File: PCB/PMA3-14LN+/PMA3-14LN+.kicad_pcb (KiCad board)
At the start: 4 copper layers, 35 x 35 mm, 26 parts, among them U1 PMA3-14LN+, U2 L7806

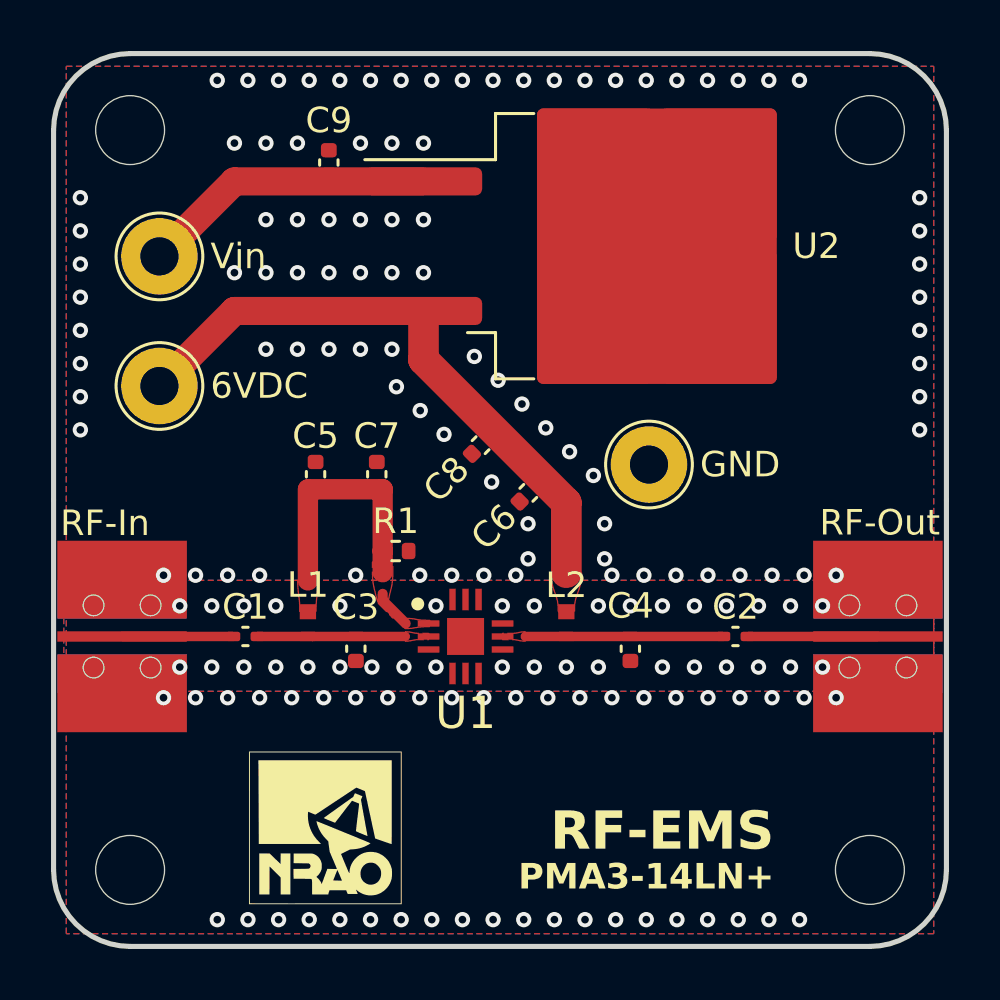
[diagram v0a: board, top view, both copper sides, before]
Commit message: pcb: added boms, updated readmes, changed silkscreen from dfs/ems to nmsm
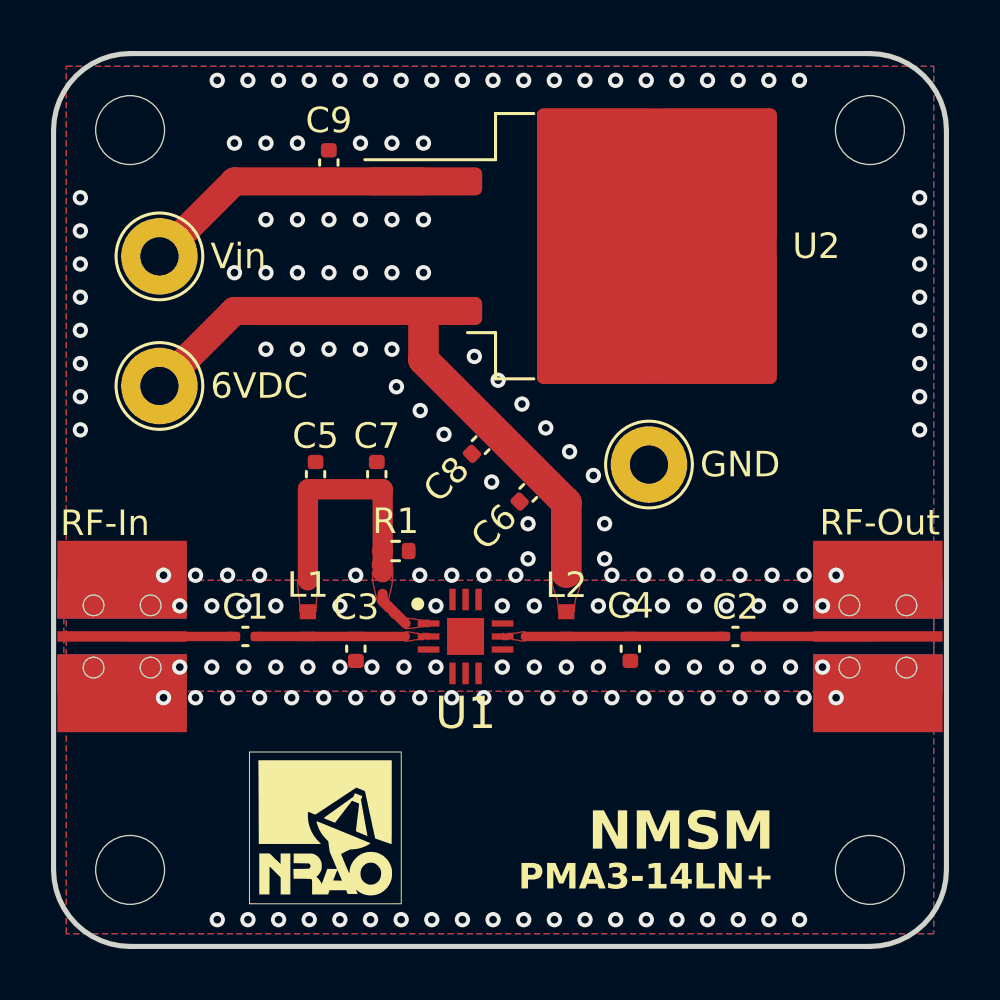
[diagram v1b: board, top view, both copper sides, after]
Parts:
- renumbered RF-In to J1, RF-Out to J2, GND to TP1, Vin to TP2, 6VDC to TP3
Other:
- board text added: "NMSM"
- board text removed: "RF-EMS"
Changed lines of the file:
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@@
     (property "ki_keywords" "test point tp")
     (attr through_hole)
-    (fp_text reference "GND" (at 2 0) (layer "F.SilkS")
+    (fp_text reference "TP1" (at 2 0) (layer "F.Fab")
         (effects (font (size 1 1) (thickness 0.15)) (justify left))
     )
@@
         (effects (font (size 1 1) (thickness 0.15)))
     )
-    (fp_text user "${REFERENCE}" (at 0.7 2.5) (layer "F.Fab")
-        (effects (font (size 1 1) (thickness 0.15)))
+    (fp_text user "GND" (at 2 0) (layer "F.SilkS")
+        (effects (font (size 1 1) (thickness 0.15)) (justify left))
     )
     (fp_circle (center 0 0) (end 1.7 0)
@@
     (property "ki_keywords" "BNC SMA SMB SMC LEMO coaxial connector CINCH RCA")
     (attr smd)
-    (fp_text reference "RF-Out" (at -4.29 4.46 180) (layer "F.SilkS")
+    (fp_text reference "J2" (at -4.29 4.46 180) (layer "F.Fab")
         (effects (font (size 1 1) (thickness 0.15)) (justify right))
     )
@@
         (effects (font (size 1 1) (thickness 0.15)))
     )
-    (fp_text user "${REFERENCE}" (at -1.5 7 180) (layer "F.Fab")
-        (effects (font (size 1 1) (thickness 0.15)))
+    (fp_text user "RF-Out" (at -4.29 4.46 180) (layer "F.SilkS")
+        (effects (font (size 1 1) (thickness 0.15)) (justify right))
     )
     (fp_circle (center -2.9718 -1.2192) (end -2.5654 -1.2192)
@@
     (property "ki_keywords" "test point tp")
     (attr through_hole)
-    (fp_text reference "6VDC" (at 2 0) (layer "F.SilkS")
+    (fp_text reference "TP3" (at 2 0) (layer "F.Fab")
         (effects (font (size 1 1) (thickness 0.15)) (justify left))
     )
@@
         (effects (font (size 1 1) (thickness 0.15)))
     )
-    (fp_text user "${REFERENCE}" (at 0.7 2.5) (layer "F.Fab")
-        (effects (font (size 1 1) (thickness 0.15)))
+    (fp_text user "6VDC" (at 2 0) (layer "F.SilkS")
+        (effects (font (size 1 1) (thickness 0.15)) (justify left))
     )
     (fp_circle (center 0 0) (end 1.7 0)
@@
     (property "ki_keywords" "test point tp")
     (attr through_hole)
-    (fp_text reference "Vin" (at 2 0) (layer "F.SilkS")
+    (fp_text reference "TP2" (at 2 0) (layer "F.Fab")
         (effects (font (size 1 1) (thickness 0.15)) (justify left))
     )
@@
         (effects (font (size 1 1) (thickness 0.15)))
     )
-    (fp_text user "${REFERENCE}" (at 0.7 2.5) (layer "F.Fab")
-        (effects (font (size 1 1) (thickness 0.15)))
+    (fp_text user "Vin" (at 2 0) (layer "F.SilkS")
+        (effects (font (size 1 1) (thickness 0.15)) (justify left))
     )
     (fp_circle (center 0 0) (end 1.7 0)
@@
     (property "ki_keywords" "BNC SMA SMB SMC LEMO coaxial connector CINCH RCA")
     (attr smd)
-    (fp_text reference "RF-In" (at -4.28 -4.44) (layer "F.SilkS")
+    (fp_text reference "J1" (at -4.28 -4.44) (layer "F.Fab")
         (effects (font (size 1 1) (thickness 0.15)) (justify left))
     )
@@
         (effects (font (size 1 1) (thickness 0.15)))
     )
-    (fp_text user "${REFERENCE}" (at -1.5 7) (layer "F.Fab")
-        (effects (font (size 1 1) (thickness 0.15)))
+    (fp_text user "RF-In" (at -4.28 -4.44) (layer "F.SilkS")
+        (effects (font (size 1 1) (thickness 0.15)) (justify left))
     )
     (fp_circle (center -2.9718 -1.2192) (end -2.5654 -1.2192)
@@
     (effects (font (size 1 1) (thickness 0.2) bold) (justify right bottom mirror))
   )
-  (gr_text "RF-EMS" (at 152.75 101.85) (layer "F.SilkS")
+  (gr_text "NMSM\n" (at 152.75 101.85) (layer "F.SilkS")
     (effects (font (size 1.5 1.5) (thickness 0.3) bold) (justify right bottom))
   )
